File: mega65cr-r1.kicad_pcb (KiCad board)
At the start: 4 copper layers, 435 x 140.6 mm, 208 parts, among them J1 DB9_Male_MountingHoles, J10 685119134923, J11 CON-SOCJ-2155, J12 Header for power lead to QMTE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, J13 Conn_01x04_Male, J14 Conn_02x17_Odd_Even, J15 696101000002 Fuse Holder 20mm, J16 Conn_01x04_Male, J17 C64_Tape_Port, J18 BA60BC0WT, J19 C64_User_Port, J2 DB9_Male_MountingHoles, J20 C64_Expansion_Port, J21 Audio Header, J22 DB15_Female_HighDensity_Mount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, J23 Audio Out, J24 Component A/V, J25 Joystick Ports Mezannine Lower, J26 Joystick Ports Mezannine Upper, J27 USB Blaster JTAG, J28 UART, J3 Wuerth_7499010121A, J30 Keyboard JTAG header, J4 QMTECH FPGA Module U4, J5 QMTECH FPGA Module U5, J6 SDF-60J for IEC 1541 serial p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, J7 QMTECH JTAG, J8 RTC, J9 1140084168 microSD Card Slot, P1 Full-side CD Card Slot, SW1 Reset Button, SW2 SW_SPDT_with_shield, U1 74LS373, U10 74LS06N, U11 74LS06N, U12 DP83826, U13 74LVC374, U14 PTN3363BSMP, U15 LM2678T-5.0, U16 74LVC374, U17 74LVC374, U18 74LS374, U19 74LS374, U2 74LVC374, U20 74LS125, U21 74LS125, U22 74LS06N, U23 74LVC374, U24 74LS125, U25 74LS374, U26 74LS374, U27 74LS138, U28 74LS138, U29 74LS137, U3 74LVC374, U30 74LS137, U31 74LS04, U32 74LVC374, U33 74LVC374, U34 74LVC374, U35 74LS374, U36 74LS374, U37 74LS374, U38 74LVC374, U39 74LVC374, U4 74LS373, U40 74LS374, U41 74LS374, U43 74LVC374, U44 74LS374, U5 74LS06N, U6 74LVC374, U7 74LVC374, U8 74LS374, U9 74LS373

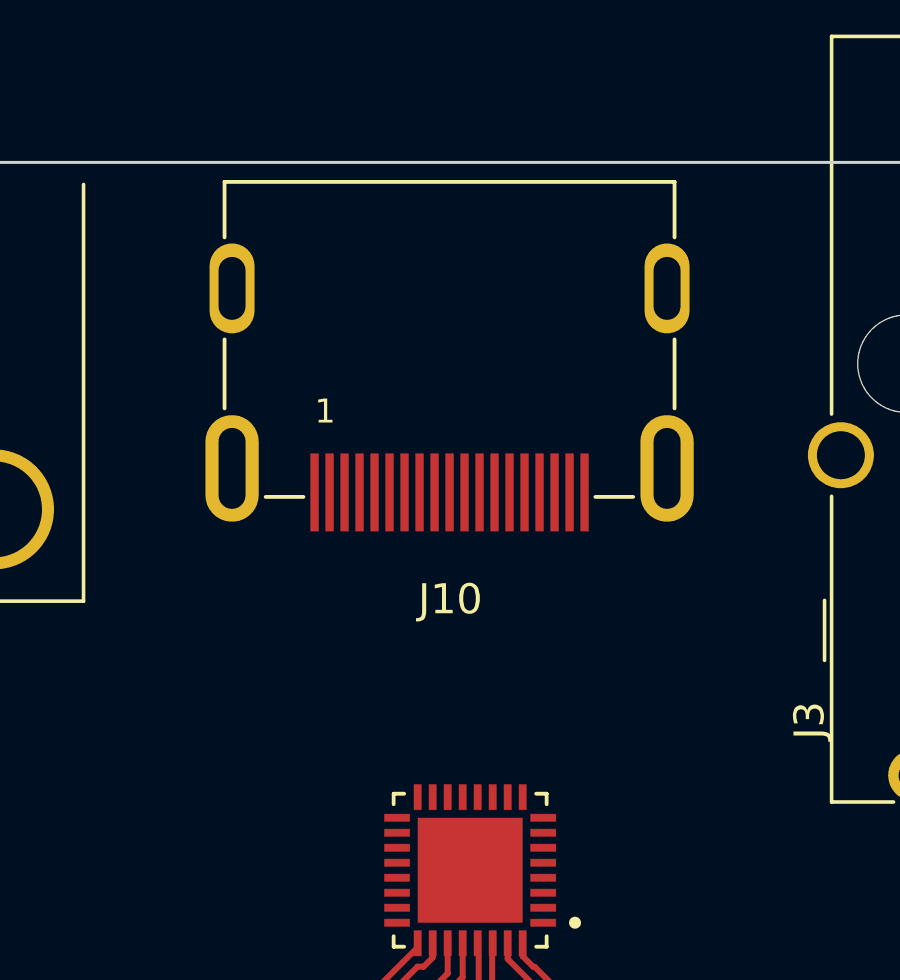
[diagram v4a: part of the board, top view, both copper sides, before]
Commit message: route HDMI connector to HDMI helper chip #13
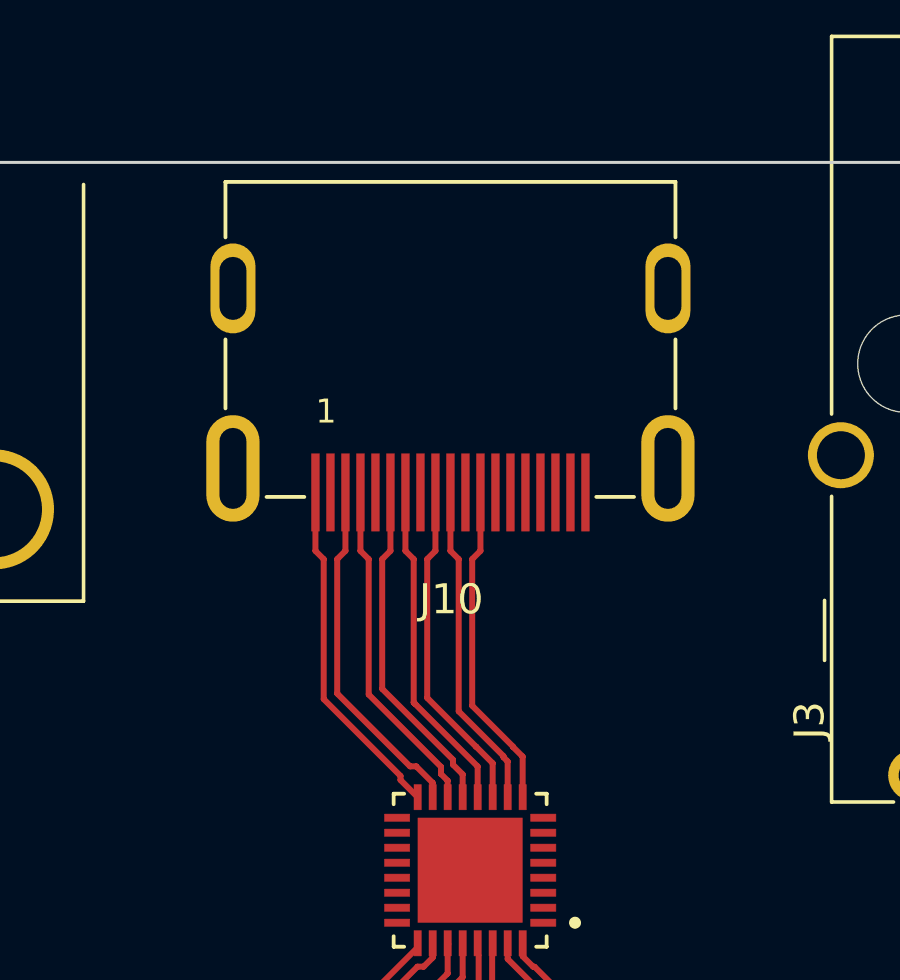
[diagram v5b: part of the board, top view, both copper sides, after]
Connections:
- J4 pad 29: HDMI_CK- -> HDMI_CK+
- J4 pad 30: HDMI_CK+ -> HDMI_CK-
- J4 pad 31: HDMI_D0- -> HDMI_D0+
- J4 pad 32: HDMI_D0+ -> HDMI_D0-
- J4 pad 33: HDMI_D1- -> HDMI_D1+
- J4 pad 34: HDMI_D1+ -> HDMI_D1-
- J4 pad 35: HDMI_D2- -> HDMI_D2+
- J4 pad 36: HDMI_D2+ -> HDMI_D2-
- U14 pad 10: /MEGA65 Peripherals, DVI, Eth, microSD/CK- -> /MEGA65 Peripherals, DVI, Eth, microSD/CK+
- U14 pad 11: /MEGA65 Peripherals, DVI, Eth, microSD/D0+ -> /MEGA65 Peripherals, DVI, Eth, microSD/D0-
- U14 pad 12: /MEGA65 Peripherals, DVI, Eth, microSD/D0- -> /MEGA65 Peripherals, DVI, Eth, microSD/D0+
- U14 pad 13: /MEGA65 Peripherals, DVI, Eth, microSD/D1+ -> /MEGA65 Peripherals, DVI, Eth, microSD/D1-
- U14 pad 14: /MEGA65 Peripherals, DVI, Eth, microSD/D1- -> /MEGA65 Peripherals, DVI, Eth, microSD/D1+
- U14 pad 15: /MEGA65 Peripherals, DVI, Eth, microSD/D2+ -> /MEGA65 Peripherals, DVI, Eth, microSD/D2-
- U14 pad 16: /MEGA65 Peripherals, DVI, Eth, microSD/D2- -> /MEGA65 Peripherals, DVI, Eth, microSD/D2+
- U14 pad 25: HDMI_D2- -> HDMI_D2+
- U14 pad 26: HDMI_D2+ -> HDMI_D2-
- U14 pad 27: HDMI_D1- -> HDMI_D1+
- U14 pad 28: HDMI_D1+ -> HDMI_D1-
- U14 pad 29: HDMI_D0- -> HDMI_D0+
- U14 pad 30: HDMI_D0+ -> HDMI_D0-
- U14 pad 31: HDMI_CK- -> HDMI_CK+
- U14 pad 32: HDMI_CK+ -> HDMI_CK-
- U14 pad 9: /MEGA65 Peripherals, DVI, Eth, microSD/CK+ -> /MEGA65 Peripherals, DVI, Eth, microSD/CK-
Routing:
- net /MEGA65 Peripherals, DVI, Eth, microSD/D2-: track 0.00 -> 11.7 mm
- net /MEGA65 Peripherals, DVI, Eth, microSD/D2+: track 0.00 -> 11.6 mm
- net /MEGA65 Peripherals, DVI, Eth, microSD/D1-: track 0.00 -> 11.4 mm
- net /MEGA65 Peripherals, DVI, Eth, microSD/D1+: track 0.00 -> 11.4 mm
- net /MEGA65 Peripherals, DVI, Eth, microSD/D0+: track 0.00 -> 11.2 mm
- net /MEGA65 Peripherals, DVI, Eth, microSD/D0-: track 0.00 -> 11.2 mm
- net /MEGA65 Peripherals, DVI, Eth, microSD/CK-: track 0.00 -> 11.0 mm
- net /MEGA65 Peripherals, DVI, Eth, microSD/CK+: track 0.00 -> 10.9 mm
- net HDMI_D0-: track 17.3 -> 20.2 mm
- net HDMI_D0+: track 20.2 -> 17.3 mm
